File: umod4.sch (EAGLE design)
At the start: 101 parts, among them IC1 27C256-FEED-THRU, M1 Generic single-sided NEO-8, M2 RPi Pico W, Q1 DNP/SI2301CDS, Q2 SS8050, U1 RP2040, U2 W25Q128JVSIQ, U3 SY6280AAC, U4 74LVC2G04, U5 74LVC541, U6 74LVC541, U7 74LVC4245, U8 TLV75733P, Y1 12MHz

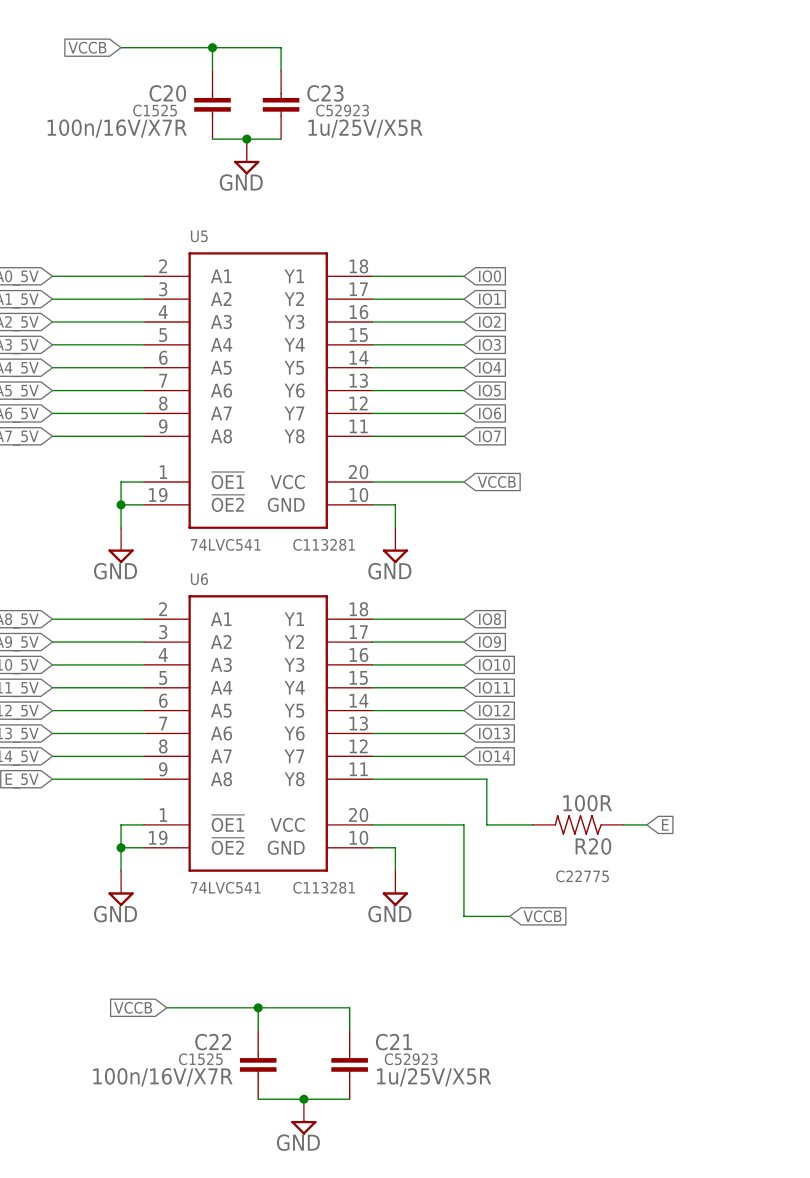
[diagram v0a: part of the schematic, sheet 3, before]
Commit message: Replace 1uF 0402 packages with SMD-0402-NOM
- Affected parts: C21, C23
- LCSC_PART unchanged
- Manually reworked wire angles on board to clear DRC failures from the new pad geometry
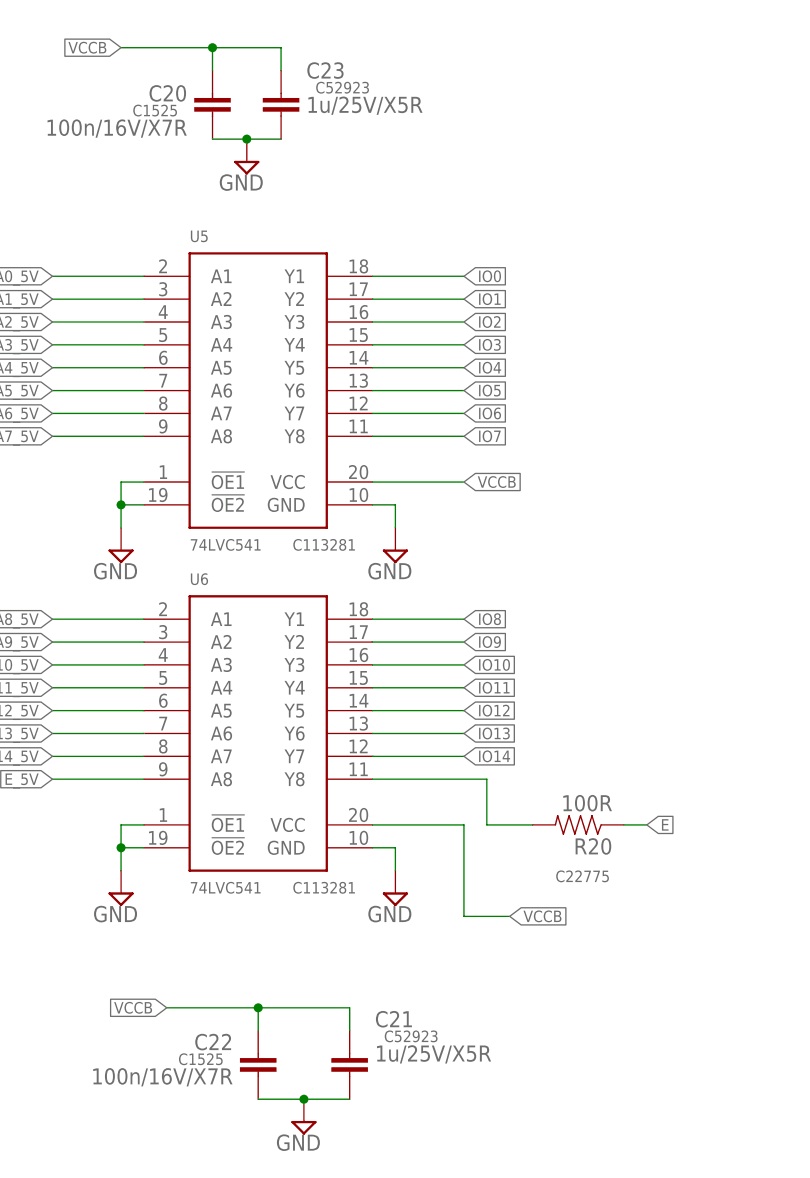
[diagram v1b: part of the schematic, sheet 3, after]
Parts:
- C21, C23: device SparkFun-03-01-2010:CAP0402-CAP -> robins-v7:CAP-0402-NOM
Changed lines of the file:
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@@
 <attribute name="LCSC_PART" value="C1525"/>
 </part>
-<part name="C23" library="SparkFun-03-01-2010" deviceset="CAP" device="0402-CAP" value="1u/25V/X5R">
+<part name="C23" library="robins-v7" deviceset="CAP" device="-0402-NOM" value="1u/25V/X5R">
 <attribute name="LCSC_PART" value="C52923"/>
 </part>
@@
 <attribute name="LCSC_PART" value="C1525"/>
 </part>
-<part name="C21" library="SparkFun-03-01-2010" deviceset="CAP" device="0402-CAP" value="1u/25V/X5R">
+<part name="C21" library="robins-v7" deviceset="CAP" device="-0402-NOM" value="1u/25V/X5R">
 <attribute name="LCSC_PART" value="C52923"/>
 </part>
@@
 <attribute name="LCSC_PART" x="52.07" y="143.51" size="1.27" layer="96" rot="R180"/>
 </instance>
-<instance part="C23" gate="G$1" x="63.5" y="142.24" smashed="yes">
-<attribute name="NAME" x="66.294" y="143.891" size="1.778" layer="95"/>
-<attribute name="VALUE" x="66.294" y="140.081" size="1.778" layer="96"/>
-<attribute name="LCSC_PART" x="67.31" y="142.24" size="1.27" layer="96"/>
+<instance part="C23" gate="G$1" x="63.5" y="144.78" smashed="yes">
+<attribute name="NAME" x="66.294" y="146.431" size="1.778" layer="95"/>
+<attribute name="VALUE" x="66.294" y="142.621" size="1.778" layer="96"/>
+<attribute name="LCSC_PART" x="67.31" y="144.78" size="1.27" layer="96"/>
 </instance>
 <instance part="C22" gate="G$1" x="60.96" y="35.56" smashed="yes">
@@
 <attribute name="LCSC_PART" x="57.15" y="38.1" size="1.27" layer="96" rot="R180"/>
 </instance>
-<instance part="C21" gate="G$1" x="71.12" y="35.56" smashed="yes">
-<attribute name="NAME" x="73.914" y="38.481" size="1.778" layer="95"/>
-<attribute name="VALUE" x="73.914" y="34.671" size="1.778" layer="96"/>
-<attribute name="LCSC_PART" x="74.93" y="36.83" size="1.27" layer="96"/>
+<instance part="C21" gate="G$1" x="71.12" y="38.1" smashed="yes">
+<attribute name="NAME" x="73.914" y="41.021" size="1.778" layer="95"/>
+<attribute name="VALUE" x="73.914" y="37.211" size="1.778" layer="96"/>
+<attribute name="LCSC_PART" x="74.93" y="39.37" size="1.27" layer="96"/>
 </instance>
 <instance part="V22" gate="GND" x="59.69" y="137.16" rot="MR0"/>

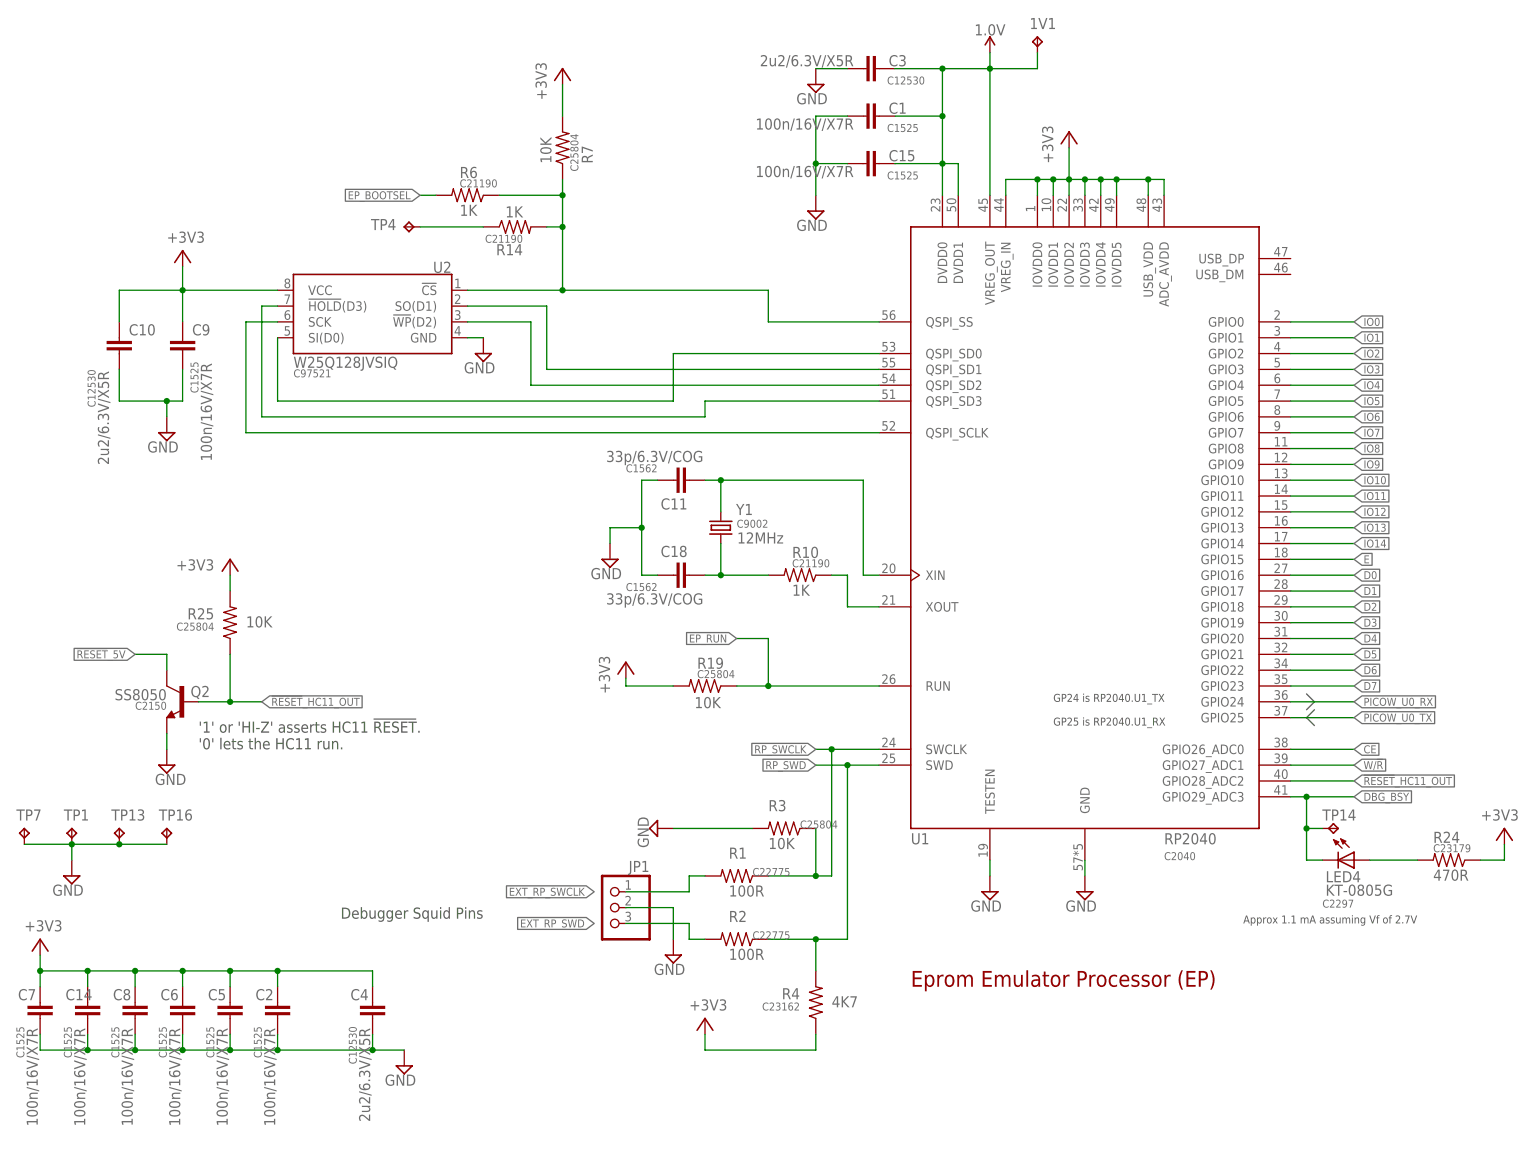
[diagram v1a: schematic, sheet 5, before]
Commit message: Replace 2.2uF 0402 packages with SMD-0402-NOM
- Affected parts: C3, C4, C10
- LCSC_PART unchanged
- Manually reworked wire angles on board to clear DRC failures from the new pad geometry
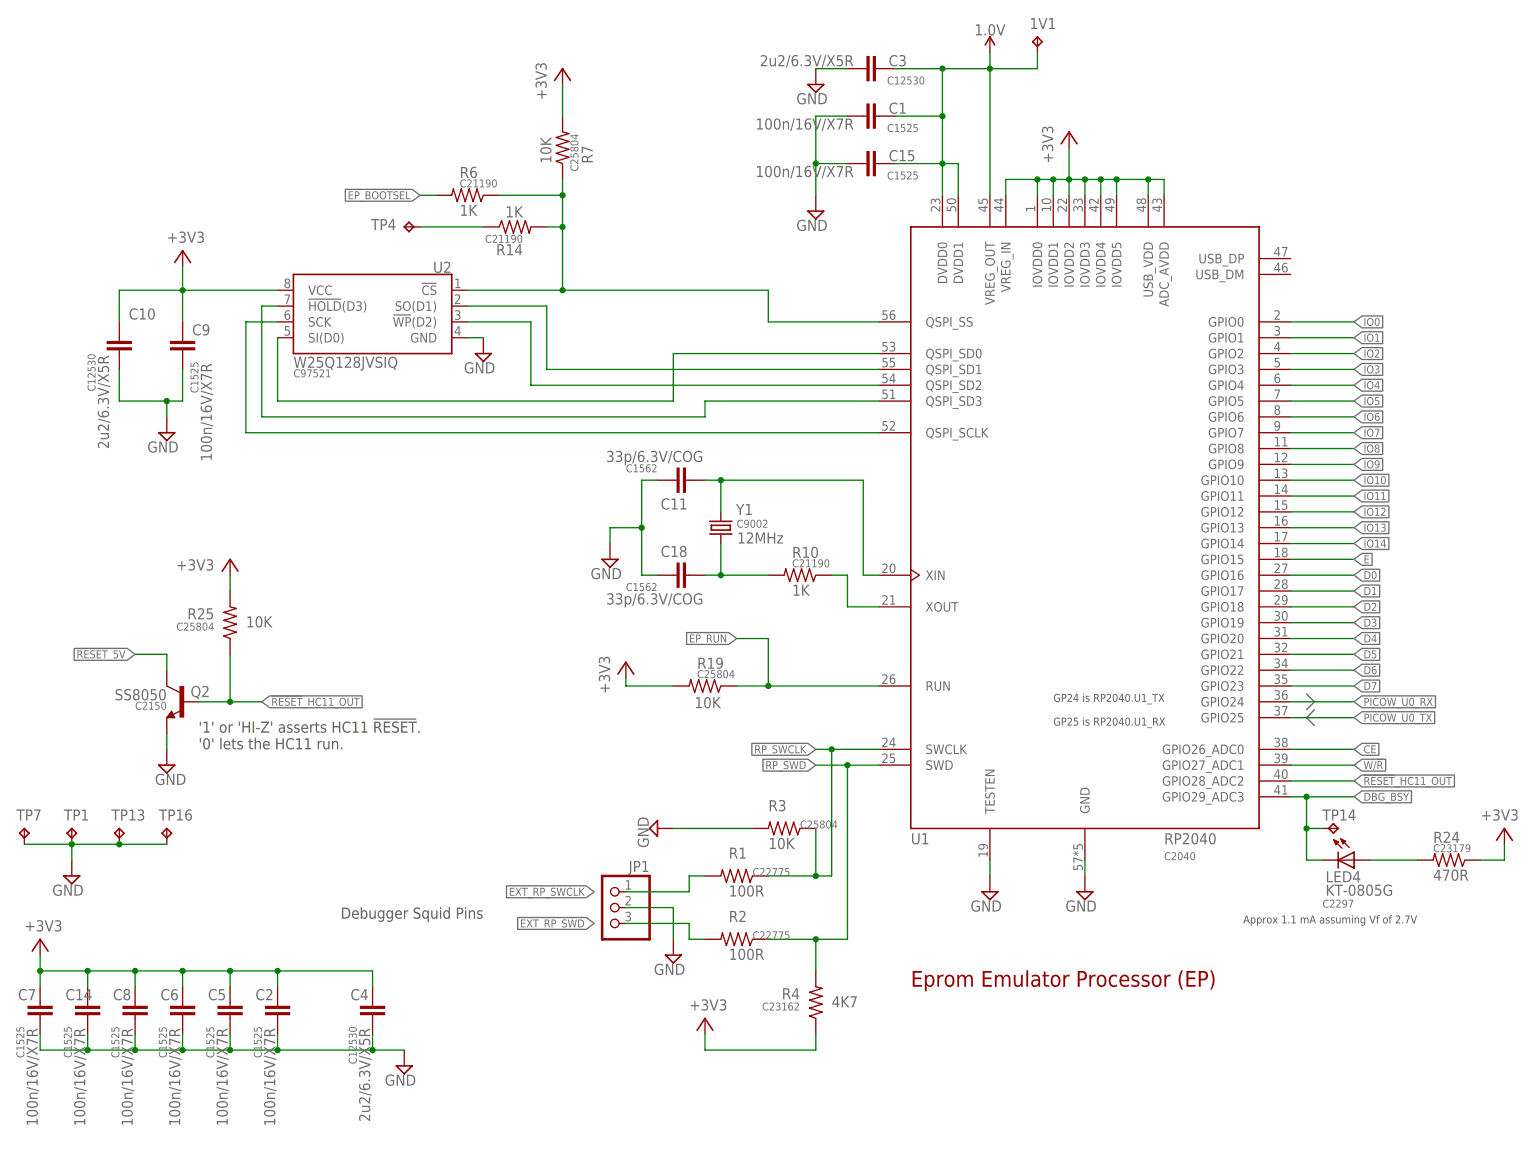
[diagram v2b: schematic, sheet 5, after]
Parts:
- C10, C3, C4: device SparkFun-03-01-2010:CAP0402-CAP -> robins-v7:CAP-0402-NOM
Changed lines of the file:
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@@
 <attribute name="LCSC_PART" value="C1525"/>
 </part>
-<part name="C10" library="SparkFun-03-01-2010" deviceset="CAP" device="0402-CAP" value="2u2/6.3V/X5R">
+<part name="C10" library="robins-v7" deviceset="CAP" device="-0402-NOM" value="2u2/6.3V/X5R">
 <attribute name="LCSC_PART" value="C12530"/>
 </part>
-<part name="C3" library="SparkFun-03-01-2010" deviceset="CAP" device="0402-CAP" value="2u2/6.3V/X5R">
+<part name="C3" library="robins-v7" deviceset="CAP" device="-0402-NOM" value="2u2/6.3V/X5R">
 <attribute name="LCSC_PART" value="C12530"/>
 </part>
 <part name="V16" library="supply2" deviceset="GND" device=""/>
-<part name="C4" library="SparkFun-03-01-2010" deviceset="CAP" device="0402-CAP" value="2u2/6.3V/X5R">
+<part name="C4" library="robins-v7" deviceset="CAP" device="-0402-NOM" value="2u2/6.3V/X5R">
 <attribute name="LCSC_PART" value="C12530"/>
 </part>
@@
 <attribute name="LCSC_PART" x="34.29" y="128.27" size="1.27" layer="96" rot="R270"/>
 </instance>
-<instance part="C10" gate="G$1" x="22.86" y="129.54" smashed="yes">
-<attribute name="NAME" x="24.384" y="132.461" size="1.778" layer="95"/>
-<attribute name="VALUE" x="19.431" y="126.746" size="1.778" layer="96" rot="R270"/>
-<attribute name="LCSC_PART" x="17.78" y="127" size="1.27" layer="96" rot="R270"/>
-</instance>
-<instance part="C3" gate="G$1" x="142.24" y="175.26" smashed="yes" rot="R270">
+<instance part="C10" gate="G$1" x="22.86" y="132.08" smashed="yes">
+<attribute name="NAME" x="24.384" y="135.001" size="1.778" layer="95"/>
+<attribute name="VALUE" x="19.431" y="129.286" size="1.778" layer="96" rot="R270"/>
+<attribute name="LCSC_PART" x="17.78" y="129.54" size="1.27" layer="96" rot="R270"/>
+</instance>
+<instance part="C3" gate="G$1" x="144.78" y="175.26" smashed="yes" rot="R270">
 <attribute name="NAME" x="146.304" y="175.641" size="1.778" layer="95"/>
 <attribute name="VALUE" x="140.716" y="177.419" size="1.778" layer="96" rot="R180"/>
@@
 </instance>
 <instance part="V16" gate="GND" x="134.62" y="172.72" rot="MR0"/>
-<instance part="C4" gate="G$1" x="63.5" y="22.86" smashed="yes">
+<instance part="C4" gate="G$1" x="63.5" y="25.4" smashed="yes">
 <attribute name="NAME" x="59.944" y="25.781" size="1.778" layer="95"/>
 <attribute name="VALUE" x="61.341" y="21.336" size="1.778" layer="96" rot="R270"/>
@@
 <junction x="40.64" y="17.78"/>
 <pinref part="C4" gate="G$1" pin="2"/>
+<junction x="48.26" y="17.78"/>
 <wire x1="48.26" y1="17.78" x2="63.5" y2="17.78" width="0.1524" layer="91"/>
-<wire x1="63.5" y1="17.78" x2="63.5" y2="20.32" width="0.1524" layer="91"/>
-<junction x="48.26" y="17.78"/>
+<wire x1="63.5" y1="17.78" x2="68.58" y2="17.78" width="0.1524" layer="91"/>
+<wire x1="63.5" y1="20.32" x2="63.5" y2="17.78" width="0.1524" layer="91"/>
 <junction x="63.5" y="17.78"/>
-<wire x1="63.5" y1="17.78" x2="68.58" y2="17.78" width="0.1524" layer="91"/>
-</segment>
-<segment>
+</segment>
+<segment>

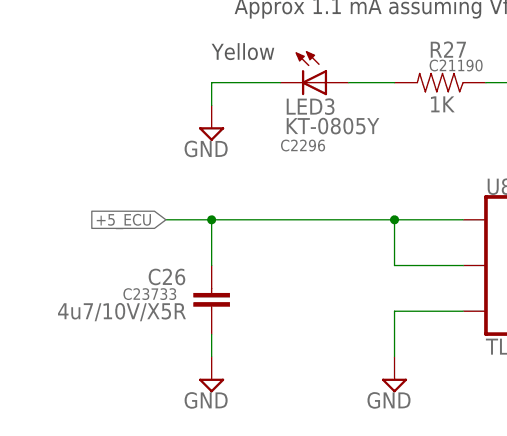
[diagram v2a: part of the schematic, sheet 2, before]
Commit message: Replace 4u7 0402 packages with SMD-0402-NOM
- Affected parts: C13, C26
- LCSC_PART unchanged
- Manually reworked wire angles on board to clear DRC failures from the new pad geometry
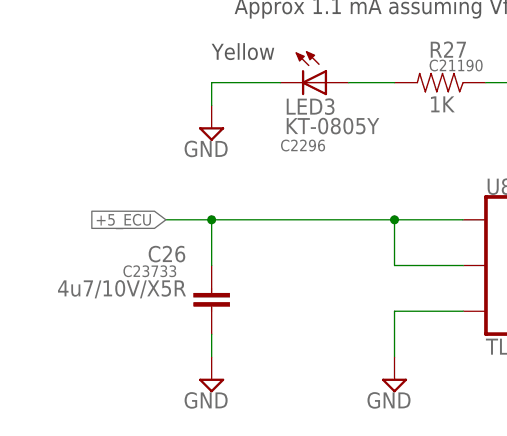
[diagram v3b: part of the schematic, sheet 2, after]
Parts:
- C13, C26: device SparkFun-03-01-2010:CAP0402-CAP -> robins-v7:CAP-0402-NOM
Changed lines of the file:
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@@
 </part>
 <part name="V11" library="supply2" deviceset="GND" device=""/>
-<part name="C13" library="SparkFun-03-01-2010" deviceset="CAP" device="0402-CAP" value="4u7/10V/X5R">
+<part name="C13" library="robins-v7" deviceset="CAP" device="-0402-NOM" value="4u7/10V/X5R">
 <attribute name="LCSC_PART" value="C23733"/>
 </part>
@@
 <part name="TP3" library="robins-v7" deviceset="TEST-POINT" device="-1035" value="1035"/>
 <part name="V48" library="supply2" deviceset="GND" device=""/>
-<part name="C26" library="SparkFun-03-01-2010" deviceset="CAP" device="0402-CAP" value="4u7/10V/X5R">
+<part name="C26" library="robins-v7" deviceset="CAP" device="-0402-NOM" value="4u7/10V/X5R">
 <attribute name="LCSC_PART" value="C23733"/>
 </part>
@@
 <attribute name="LCSC_PART" x="62.23" y="62.23" size="1.27" layer="96"/>
 </instance>
-<instance part="C26" gate="G$1" x="38.1" y="35.56" smashed="yes">
-<attribute name="NAME" x="35.306" y="40.259" size="1.778" layer="95" rot="R180"/>
-<attribute name="VALUE" x="35.306" y="36.449" size="1.778" layer="96" rot="R180"/>
-<attribute name="LCSC_PART" x="34.29" y="38.1" size="1.27" layer="96" rot="R180"/>
+<instance part="C26" gate="G$1" x="38.1" y="38.1" smashed="yes">
+<attribute name="NAME" x="35.306" y="42.799" size="1.778" layer="95" rot="R180"/>
+<attribute name="VALUE" x="35.306" y="38.989" size="1.778" layer="96" rot="R180"/>
+<attribute name="LCSC_PART" x="34.29" y="40.64" size="1.27" layer="96" rot="R180"/>
 </instance>
 <instance part="C24" gate="G$1" x="93.98" y="40.64" smashed="yes">
@@
 </instance>
 <instance part="V11" gate="GND" x="134.62" y="85.09"/>
-<instance part="C13" gate="G$1" x="127" y="96.52" smashed="yes">
+<instance part="C13" gate="G$1" x="127" y="99.06" smashed="yes">
 <attribute name="NAME" x="124.206" y="101.219" size="1.778" layer="95" rot="R180"/>
 <attribute name="VALUE" x="124.206" y="97.409" size="1.778" layer="96" rot="R180"/>
